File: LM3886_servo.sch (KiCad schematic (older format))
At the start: 2 parts, among them U1 LM3886, U2 TL072

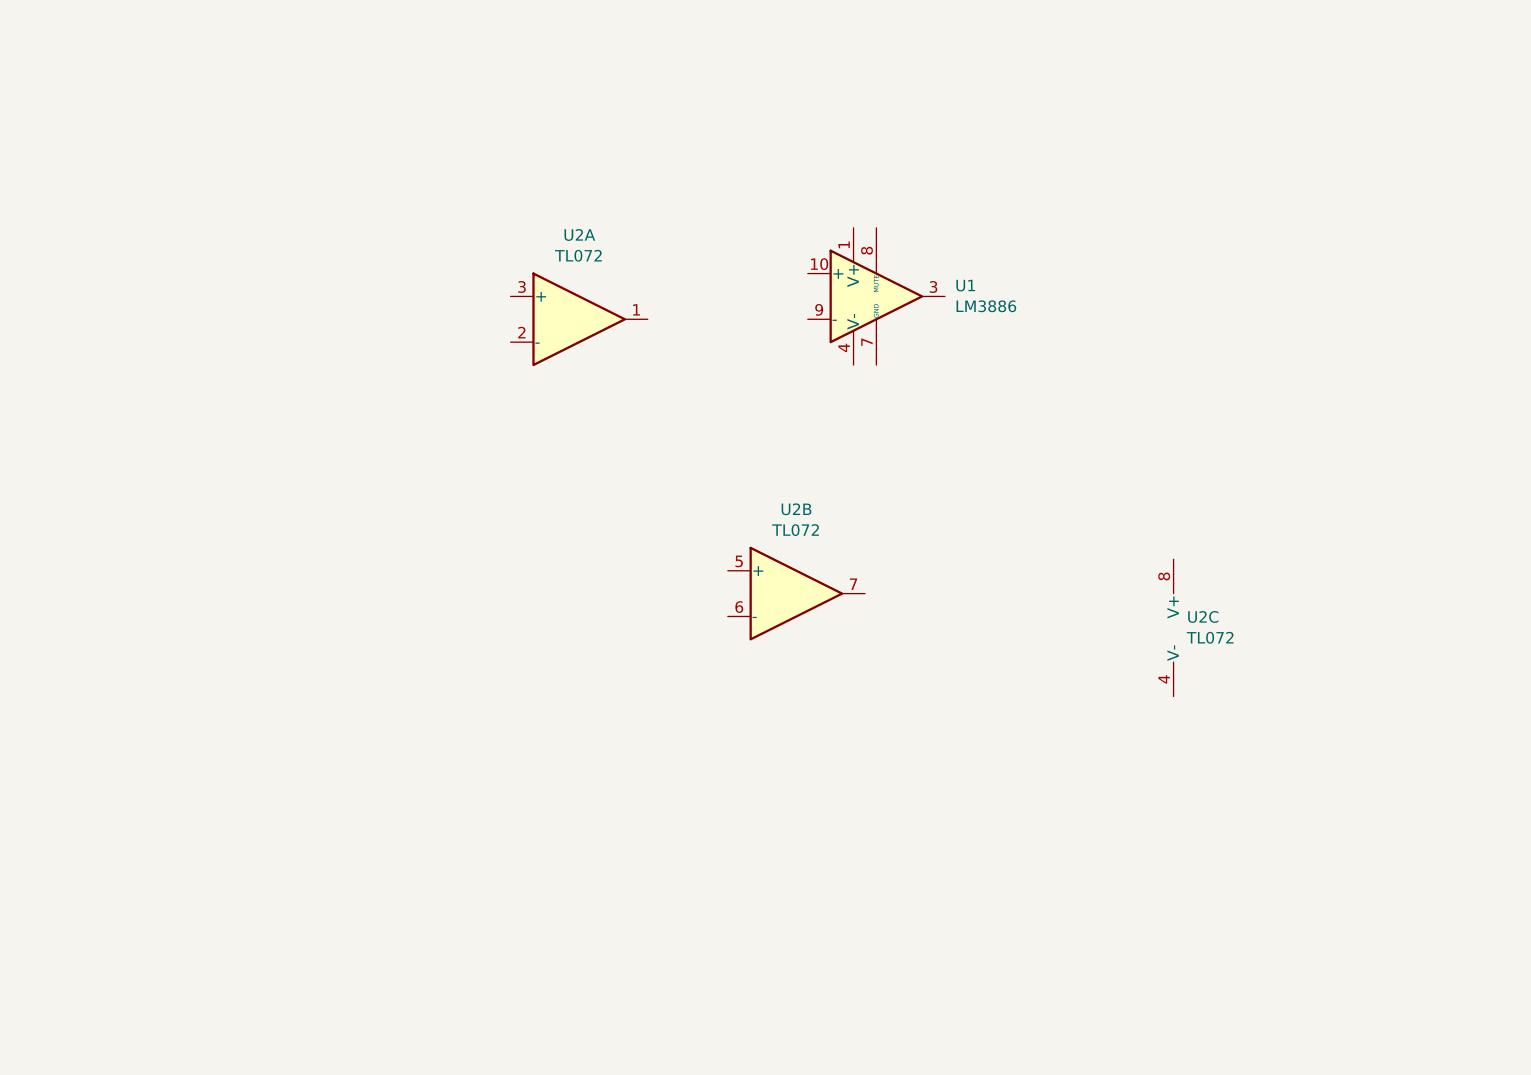
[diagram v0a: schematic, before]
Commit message: finished sch and started pcb layout
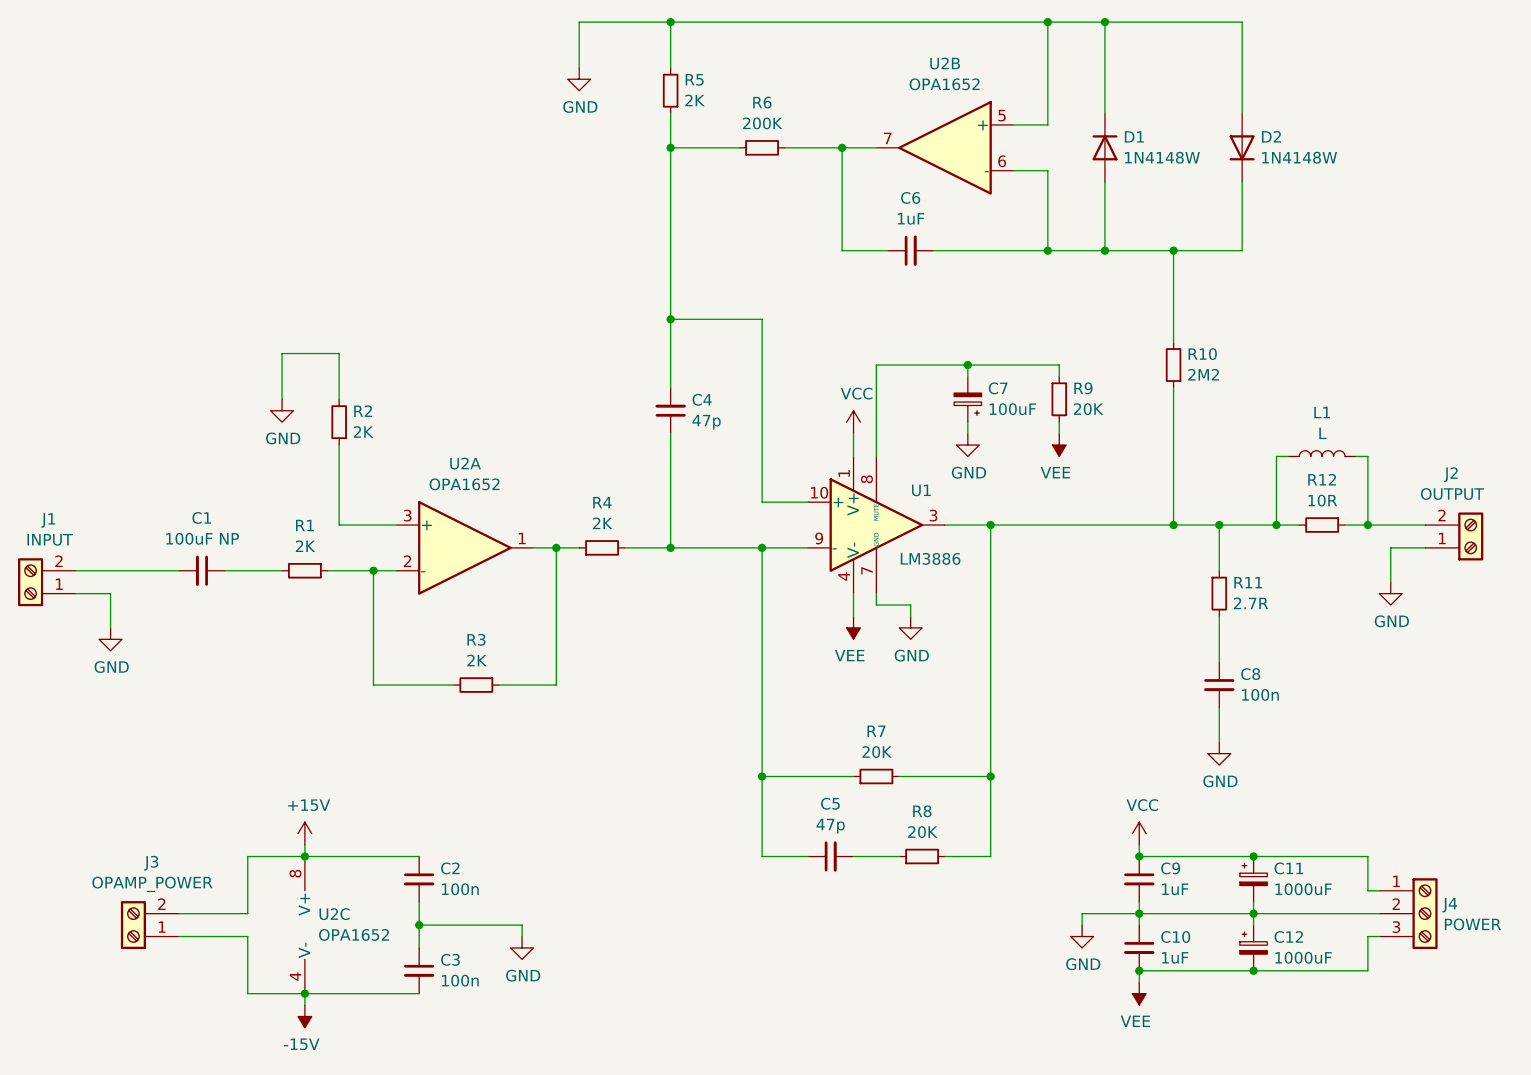
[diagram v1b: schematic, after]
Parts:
- added C1: 100uF NP, Capacitor_THT:C_Radial_D10.0mm_H16.0mm_P5.00mm, symbol Device:C_Small
- added C10, C9: 1uF, Capacitor_SMD:C_1206_3216Metric_Pad1.42x1.75mm_HandSolder, symbol Device:C_Small
- added C11, C12: 1000uF, Capacitor_THT:CP_Radial_D16.0mm_P7.50mm, symbol Device:CP_Small
- added C2, C3: 100n, Capacitor_SMD:C_1206_3216Metric_Pad1.42x1.75mm_HandSolder, symbol Device:C_Small
- added C4, C5: 47p, Capacitor_SMD:C_0805_2012Metric_Pad1.15x1.40mm_HandSolder, symbol Device:C_Small
- added C6: 1uF, Capacitor_THT:C_Rect_L7.2mm_W4.5mm_P5.00mm_FKS2_FKP2_MKS2_MKP2, symbol Device:C_Small
- added C7: 100uF, Capacitor_THT:CP_Radial_D8.0mm_P3.50mm, symbol Device:CP_Small
- added C8: 100n, Capacitor_THT:C_Rect_L7.2mm_W2.5mm_P5.00mm_FKS2_FKP2_MKS2_MKP2, symbol Device:C_Small
- added D1, D2: 1N4148W, Diode_SMD:D_SOD-123, symbol Diode:1N4148W
- added J1: INPUT, local_footprints:TerminalBlock_ Amphenol_01_02_P3.50mm, symbol Connector:Screw_Terminal_01x02
- added J2: OUTPUT, local_footprints:TerminalBlock_CUI_01x02_P5.00mm, symbol Connector:Screw_Terminal_01x02
- added J3: OPAMP_POWER, local_footprints:TerminalBlock_ Amphenol_01_02_P3.50mm, symbol Connector:Screw_Terminal_01x02
- added J4: POWER, local_footprints:TerminalBlock_CUI_01x03_P5.00mm, symbol Connector:Screw_Terminal_01x03
- added L1: L, local_footprints:Inductor_DIY, symbol Device:L
- added R1, R2, R3, R4, R5: 2K, Resistor_SMD:R_1206_3216Metric_Pad1.42x1.75mm_HandSolder, symbol Device:R_Small
- added R10: 2M2, Resistor_SMD:R_1206_3216Metric_Pad1.42x1.75mm_HandSolder, symbol Device:R_Small
- added R11: 2.7R, Resistor_SMD:R_2512_6332Metric_Pad1.52x3.35mm_HandSolder, symbol Device:R_Small
- added R12: 10R, Resistor_SMD:R_2512_6332Metric_Pad1.52x3.35mm_HandSolder, symbol Device:R_Small
- added R6: 200K, Resistor_SMD:R_1206_3216Metric_Pad1.42x1.75mm_HandSolder, symbol Device:R_Small
- added R7, R8, R9: 20K, Resistor_SMD:R_1206_3216Metric_Pad1.42x1.75mm_HandSolder, symbol Device:R_Small
- U2: value TL072 -> OPA1652; footprint (none) -> Package_SO:SOIC-8_3.9x4.9mm_P1.27mm
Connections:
- net VCC: now reaches U1.1 (V+), U1.5 (V+)
- net VCC: now also C11.1, C9.1, J4.1 (Pin_1)
- net at U1.10 (+): now also C4.2, R5.1, R6.1
- net at U1.3: now also L1.1, R10.1, R11.1, R12.2, R7.2, R8.2
- net VEE: now reaches U1.4 (V-)
- net VEE: now also C10.2, C12.2, J4.3 (Pin_3), R9.2
- net GND: now reaches U1.7 (GND)
- net GND: now also U2.5 (+), C10.1, C11.2, C12.1, C2.2, C3.1, C7.1, C8.2, C9.2, D1.1 (K), D2.2 (A), J1.1 (Pin_1), J2.1 (Pin_1), J4.2 (Pin_2), R2.2, R5.2
- net at U1.8 (MUTE): now also C7.2, R9.1
- net at U1.9 (-): now also C4.1, C5.1, R4.2, R7.1
- net at U2.1: now also R3.1, R4.1
- net at U2.2 (-): now also R1.1, R3.2
- net at U2.3 (+): now also R2.1
- net at U2.6 (-): now also C6.2, D1.2 (A), D2.1 (K), R10.2
- net at U2.7: now also C6.1, R6.2
- net -15V: now reaches U2.4 (V-)
- net -15V: now also C3.2, J3.1 (Pin_1)
- net +15V: now reaches U2.8 (V+)
- net +15V: now also C2.1, J3.2 (Pin_2)
- new net: C1.1, R1.2
- new net: C1.2, J1.2 (Pin_2)
- new net: C5.2, R8.1
- new net: C8.1, R11.2
- new net: J2.2 (Pin_2), L1.2, R12.1
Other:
- moved on the sheet: U1, U2A, U2B, U2C
